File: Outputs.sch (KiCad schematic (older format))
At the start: 6 parts, among them Q7 VND14NV04

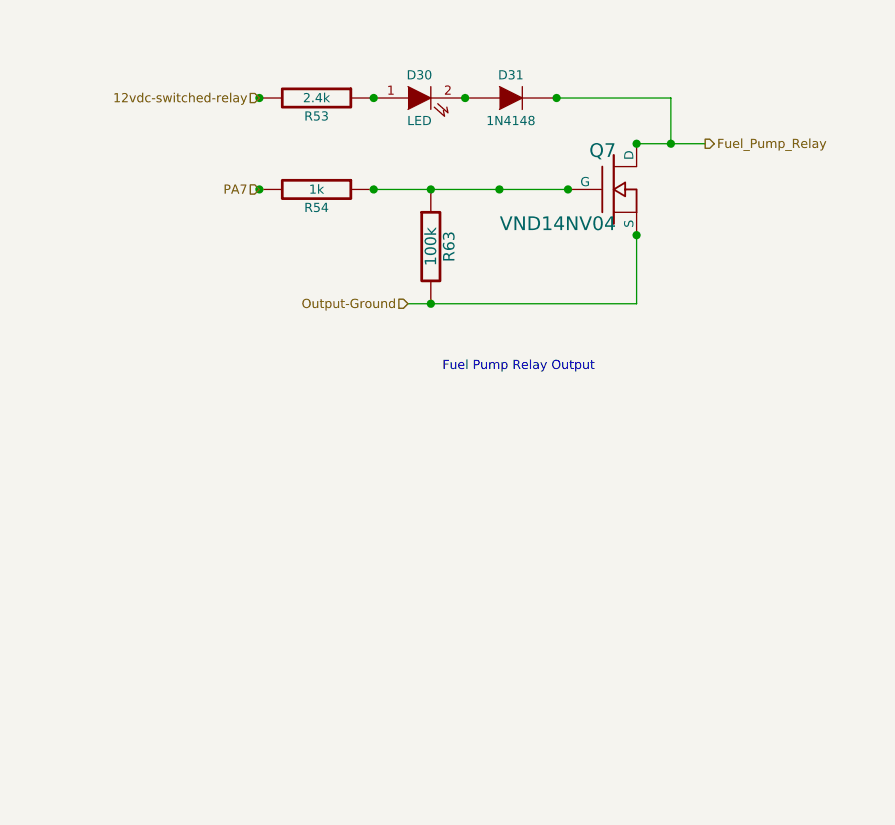
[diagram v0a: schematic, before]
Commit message: Updated Schematics, PDF, BOM for 4cyl Sequential Injection
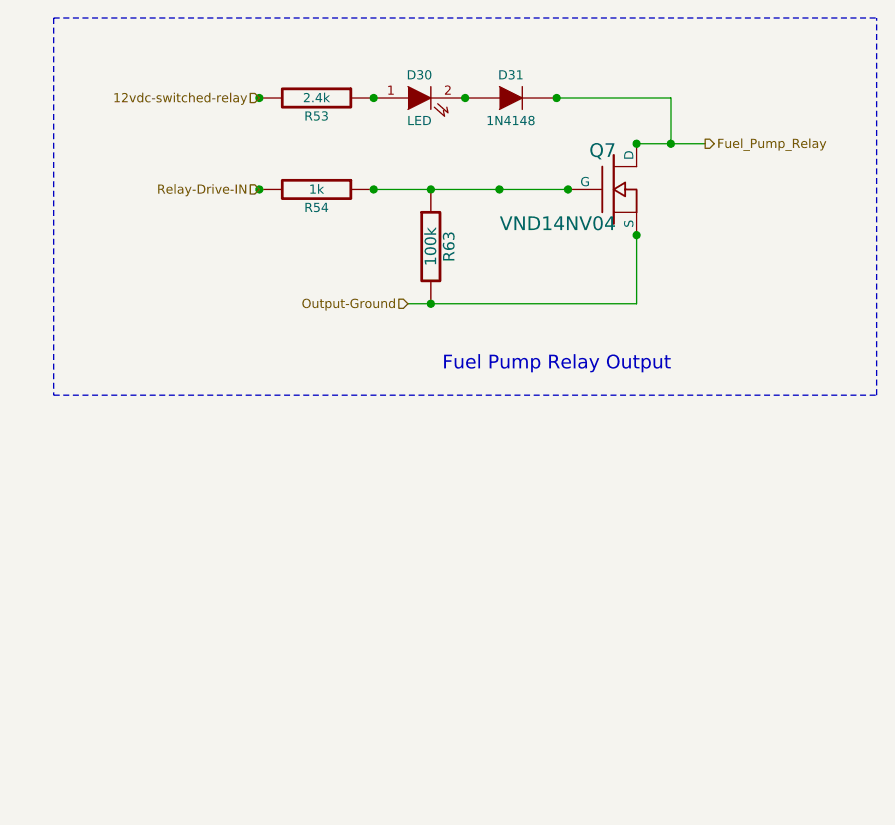
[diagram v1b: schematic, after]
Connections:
- net PA7 renamed Relay-Drive-IN
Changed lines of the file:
@@
-EESchema Schematic File Version 2  date Tue 24 Jan 2012 02:18:15 PM EST
+EESchema Schematic File Version 2  date Tue 24 Jan 2012 11:15:10 PM EST
 LIBS:power
 LIBS:device
@@
 Sheet 5 7
 Title "Jaguar PCB for FreeEMS"
-Date "24 jan 2012"
+Date "25 jan 2012"
 Rev "A.1"
 Comp "diyefi.org"
@@
 Comment4 ""
 $EndDescr
+Wire Notes Line
+	3800 2750 7400 2750
+Wire Notes Line
+	3800 2750 3800 4400
+Wire Notes Line
+	3800 4400 7400 4400
+Wire Notes Line
+	7400 4400 7400 2750
 Wire Wire Line
-	5350 4000 6350 4000
-Connection ~ 4700 3500
-Connection ~ 5200 3500
-Connection ~ 5450 3500
-Connection ~ 5450 4000
+	6500 3300 6500 3100
 Wire Wire Line
-	6350 4000 6350 3700
+	6350 3300 6650 3300
+Connection ~ 6500 3300
+Connection ~ 6350 3300
+Connection ~ 6350 3700
+Connection ~ 6050 3500
+Connection ~ 5750 3500
+Connection ~ 5200 3100
+Connection ~ 4700 3100
+Connection ~ 5600 3100
+Connection ~ 6000 3100
+Wire Wire Line
+	6500 3100 6000 3100
 Wire Wire Line
 	5200 3500 6050 3500
 Wire Wire Line
-	6000 3100 6500 3100
-Connection ~ 6000 3100
-Connection ~ 5600 3100
-Connection ~ 4700 3100
-Connection ~ 5200 3100
-Connection ~ 5750 3500
-Connection ~ 6050 3500
-Connection ~ 6350 3700
-Connection ~ 6350 3300
-Connection ~ 6500 3300
+	6350 3700 6350 4000
+Connection ~ 5450 4000
+Connection ~ 5450 3500
+Connection ~ 5200 3500
+Connection ~ 4700 3500
 Wire Wire Line
-	6350 3300 6650 3300
-Wire Wire Line
-	6500 3100 6500 3300
+	6350 4000 5350 4000
 Text HLabel 5350 4000 0    40   Input ~ 0
 Output-Ground
@@
 	1    0    0    -1
 $EndComp
-Text Notes 5500 4300 0    40   ~ 0
+Text Notes 5500 4300 0    60   ~ 0
 Fuel Pump Relay Output
 $Comp
@@
 $EndComp
 Text HLabel 4700 3500 0    40   Input ~ 0
-PA7
+Relay-Drive-IN
 Text HLabel 6650 3300 2    40   Output ~ 0
 Fuel_Pump_Relay

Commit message: Updated everything for up to 8 cylinder engines
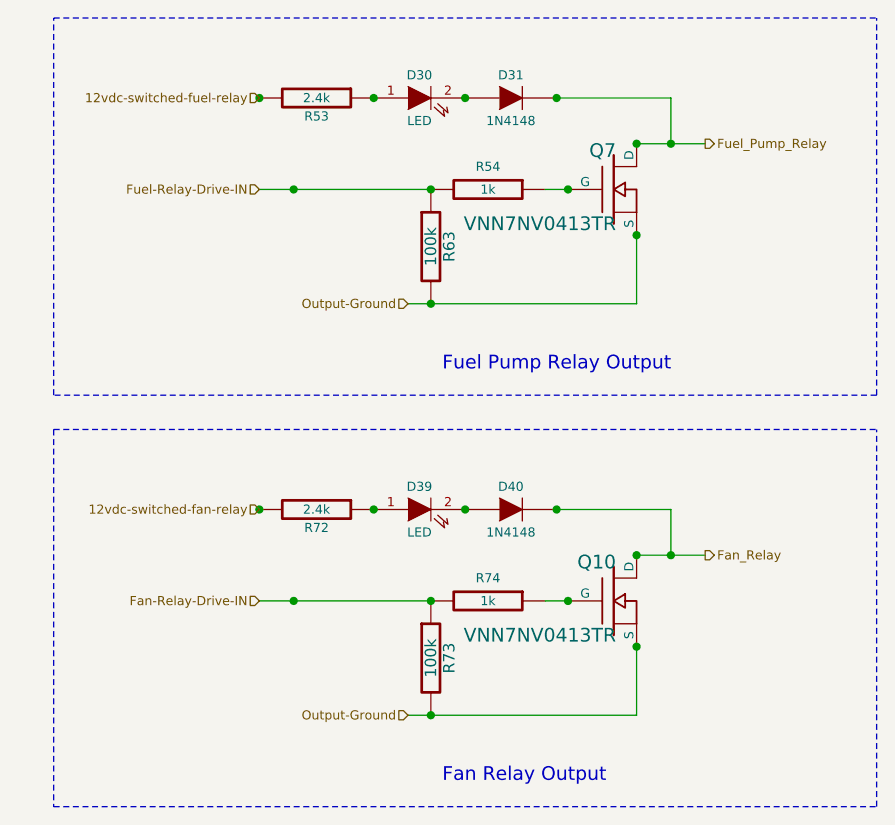
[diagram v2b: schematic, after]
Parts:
- added D39: LED, symbol LED
- added D40: 1N4148, symbol DIODE
- added Q10: VNN7NV0413TR, symbol MOSFET_N
- added R72: 2.4k, symbol R
- added R73: 100k, symbol R
- added R74: 1k, symbol R
- Q7: value VND14NV04 -> VNN7NV0413TR
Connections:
- net Output-Ground: now also Q10.S, R73.2
- net at Q7.G, R54.1: no longer R63.1
- net 12vdc-switched-relay renamed 12vdc-switched-fuel-relay
- net Relay-Drive-IN renamed Fuel-Relay-Drive-IN
- net Fuel-Relay-Drive-IN: now also R63.1
- new net: Q10.G, R74.1
- new net: D39.2 (K), D40.1 (A)
- new net: D39.1 (A), R72.1
- new net 12vdc-switched-fan-relay: R72.2
- new net Fan-Relay-Drive-IN: R73.1, R74.2
- new net Fan_Relay: D40.2 (K), Q10.D
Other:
- note added: "Fan Relay Output"
- moved on the sheet: R54
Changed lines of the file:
@@
-EESchema Schematic File Version 2  date Tue 24 Jan 2012 11:15:10 PM EST
+EESchema Schematic File Version 2  date Thu 26 Jan 2012 03:16:21 AM EST
 LIBS:power
 LIBS:device
@@
 Sheet 5 7
 Title "Jaguar PCB for FreeEMS"
-Date "25 jan 2012"
+Date "26 jan 2012"
 Rev "A.1"
 Comp "diyefi.org"
@@
 Comment4 ""
 $EndDescr
+Wire Wire Line
+	5450 5300 4700 5300
+Wire Notes Line
+	3800 4550 7400 4550
+Wire Notes Line
+	3800 4550 3800 6200
+Wire Notes Line
+	3800 6200 7400 6200
+Wire Notes Line
+	7400 6200 7400 4550
+Wire Wire Line
+	6500 5100 6500 4900
+Wire Wire Line
+	6350 5100 6650 5100
+Connection ~ 6500 5100
+Connection ~ 6350 5100
+Connection ~ 6350 5500
+Connection ~ 6050 5300
+Connection ~ 5200 4900
+Connection ~ 4700 4900
+Connection ~ 5600 4900
+Connection ~ 6000 4900
+Wire Wire Line
+	6500 4900 6000 4900
+Wire Wire Line
+	6350 5500 6350 5800
+Connection ~ 5450 5800
+Connection ~ 5450 5300
+Wire Wire Line
+	6350 5800 5350 5800
+Wire Wire Line
+	5950 5300 6050 5300
+Connection ~ 4850 5300
+Connection ~ 4850 3500
+Wire Wire Line
+	5950 3500 6050 3500
+Wire Wire Line
+	5350 4000 6350 4000
+Connection ~ 5450 3500
+Connection ~ 5450 4000
+Wire Wire Line
+	6350 4000 6350 3700
+Wire Wire Line
+	6000 3100 6500 3100
+Connection ~ 6000 3100
+Connection ~ 5600 3100
+Connection ~ 4700 3100
+Connection ~ 5200 3100
+Connection ~ 6050 3500
+Connection ~ 6350 3700
+Connection ~ 6350 3300
+Connection ~ 6500 3300
+Wire Wire Line
+	6350 3300 6650 3300
+Wire Wire Line
+	6500 3100 6500 3300
+Wire Notes Line
+	7400 4400 7400 2750
+Wire Notes Line
+	7400 4400 3800 4400
+Wire Notes Line
+	3800 4400 3800 2750
 Wire Notes Line
 	3800 2750 7400 2750
-Wire Notes Line
-	3800 2750 3800 4400
-Wire Notes Line
-	3800 4400 7400 4400
-Wire Notes Line
-	7400 4400 7400 2750
-Wire Wire Line
-	6500 3300 6500 3100
-Wire Wire Line
-	6350 3300 6650 3300
-Connection ~ 6500 3300
-Connection ~ 6350 3300
-Connection ~ 6350 3700
-Connection ~ 6050 3500
-Connection ~ 5750 3500
-Connection ~ 5200 3100
-Connection ~ 4700 3100
-Connection ~ 5600 3100
-Connection ~ 6000 3100
-Wire Wire Line
-	6500 3100 6000 3100
-Wire Wire Line
-	5200 3500 6050 3500
-Wire Wire Line
-	6350 3700 6350 4000
-Connection ~ 5450 4000
-Connection ~ 5450 3500
-Connection ~ 5200 3500
-Connection ~ 4700 3500
-Wire Wire Line
-	6350 4000 5350 4000
+Wire Wire Line
+	5450 3500 4700 3500
+$Comp
+L R R74
+U 1 1 4F20C919
+P 5700 5300
+F 0 "R74" V 5600 5300 40  0000 C CNN
+F 1 "1k" V 5700 5300 40  0000 C CNN
+	1    5700 5300
+	0    1    1    0
+$EndComp
+Text HLabel 4700 4900 0    40   Input ~ 0
+12vdc-switched-fan-relay
+Text HLabel 6650 5100 2    40   Output ~ 0
+Fan_Relay
+Text HLabel 4700 5300 0    40   Input ~ 0
+Fan-Relay-Drive-IN
+$Comp
+L R R72
+U 1 1 4F20C918
+P 4950 4900
+F 0 "R72" V 5030 4900 40  0000 C CNN
+F 1 "2.4k" V 4950 4900 40  0000 C CNN
+	1    4950 4900
+	0    1    1    0
+$EndComp
+$Comp
+L LED D39
+U 1 1 4F20C917
+P 5400 4900
+F 0 "D39" H 5400 5000 40  0000 C CNN
+F 1 "LED" H 5400 4800 40  0000 C CNN
+	1    5400 4900
+	1    0    0    -1
+$EndComp
+$Comp
+L DIODE D40
+U 1 1 4F20C916
+P 5800 4900
+F 0 "D40" H 5800 5000 40  0000 C CNN
+F 1 "1N4148" H 5800 4800 40  0000 C CNN
+	1    5800 4900
+	1    0    0    -1
+$EndComp
+Text Notes 5500 6100 0    60   ~ 0
+Fan Relay Output
+$Comp
+L MOSFET_N Q10
+U 1 1 4F20C915
+P 6250 5300
+F 0 "Q10" H 6260 5470 60  0000 R CNN
+F 1 "VNN7NV0413TR" H 6260 5150 60  0000 R CNN
+	1    6250 5300
+	1    0    0    -1
+$EndComp
+$Comp
+L R R73
+U 1 1 4F20C914
+P 5450 5550
+F 0 "R73" V 5530 5550 50  0000 C CNN
+F 1 "100k" V 5450 5550 50  0000 C CNN
+	1    5450 5550
+	1    0    0    -1
+$EndComp
+Text HLabel 5350 5800 0    40   Input ~ 0
+Output-Ground
 Text HLabel 5350 4000 0    40   Input ~ 0
 Output-Ground
@@
 P 6250 3500
 F 0 "Q7" H 6260 3670 60  0000 R CNN
-F 1 "VND14NV04" H 6260 3350 60  0000 R CNN
+F 1 "VNN7NV0413TR" H 6260 3350 60  0000 R CNN
 	1    6250 3500
 	1    0    0    -1
@@
 $EndComp
 Text HLabel 4700 3500 0    40   Input ~ 0
-Relay-Drive-IN
+Fuel-Relay-Drive-IN
 Text HLabel 6650 3300 2    40   Output ~ 0
 Fuel_Pump_Relay
 Text HLabel 4700 3100 0    40   Input ~ 0
-12vdc-switched-relay
+12vdc-switched-fuel-relay
 $Comp
 L R R54
 U 1 1 4F0744B6
-P 4950 3500
-F 0 "R54" V 5030 3500 40  0000 C CNN
-F 1 "1k" V 4950 3500 40  0000 C CNN
-	1    4950 3500
-	0    1    1    0
-$EndComp
+P 5700 3500
+F 0 "R54" V 5600 3500 40  0000 C CNN
+F 1 "1k" V 5700 3500 40  0000 C CNN
+	1    5700 3500
+	0    1    1    0
+$EndComp

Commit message: modified:   Outputs.sch
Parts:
- renumbered Q7 to Q9
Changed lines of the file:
@@
-EESchema Schematic File Version 2  date Thu 26 Jan 2012 03:16:21 AM EST
+EESchema Schematic File Version 2  date Thu 26 Jan 2012 12:42:01 PM EST
 LIBS:power
 LIBS:device
@@
 $EndComp
 $Comp
-L MOSFET_N Q7
+L MOSFET_N Q9
 U 1 1 4F19BBF5
 P 6250 3500
-F 0 "Q7" H 6260 3670 60  0000 R CNN
+F 0 "Q9" H 6260 3670 60  0000 R CNN
 F 1 "VNN7NV0413TR" H 6260 3350 60  0000 R CNN
 	1    6250 3500
